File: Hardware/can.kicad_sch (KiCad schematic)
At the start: 11 parts, among them U2 SN65HVD230

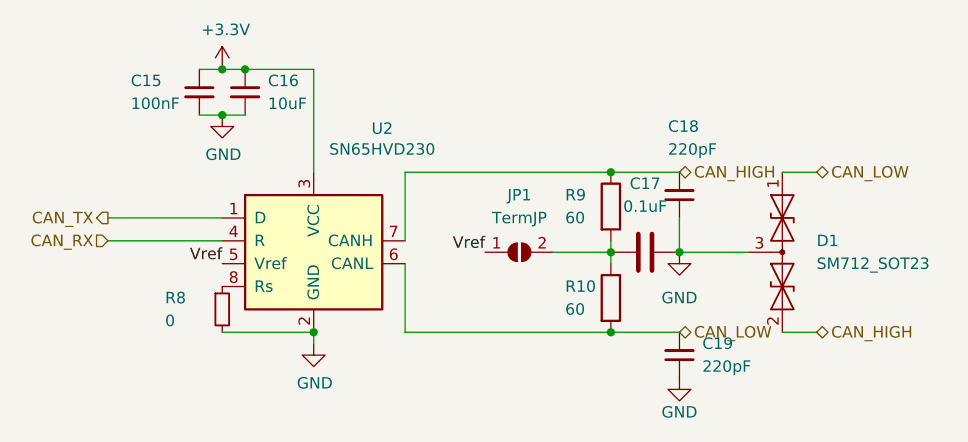
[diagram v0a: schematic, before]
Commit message: schematic done? + footprints assigned
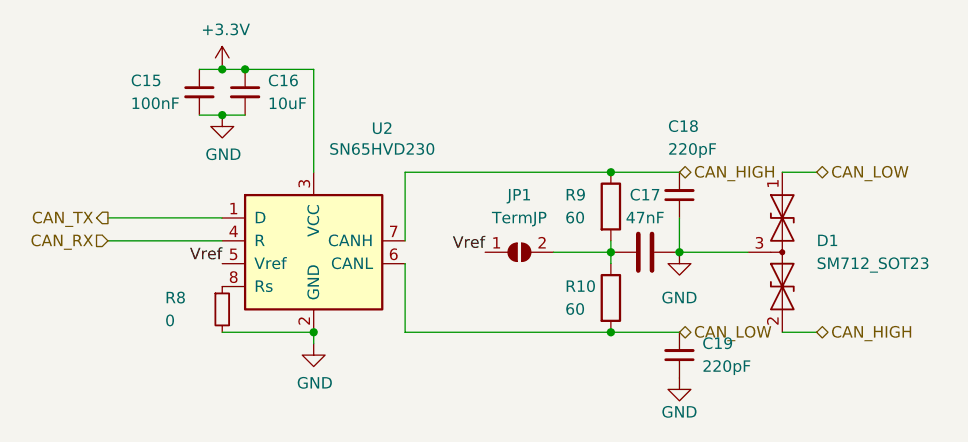
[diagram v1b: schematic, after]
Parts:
- C17: value 0.1uF -> 47nF
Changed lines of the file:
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@@
   (symbol (lib_id "Device:C") (at 171.45 88.9 90) (unit 1)
     (in_bom yes) (on_board yes) (dnp no) (fields_autoplaced)
-    (property "Reference" "C17" (at 171.45 81.28 90)
+    (property "Reference" "C17" (at 171.45 82.55 90)
       (effects (font (size 1.27 1.27)))
     )
-    (property "Value" "0.1uF" (at 171.45 83.82 90)
+    (property "Value" "47nF" (at 171.45 85.09 90)
       (effects (font (size 1.27 1.27)))
     )

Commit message: I had to get back out of bed to push this commit
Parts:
- JP1: footprint Jumper:SolderJumper-2_P1.3mm_Open_RoundedPad1.0x1.5mm -> iclr:SmallerSolderJP
- R10, R9: footprint Resistor_SMD:R_0402_1005Metric -> Resistor_SMD:R_0603_1608Metric
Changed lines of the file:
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@@
       (effects (font (size 1.27 1.27)) (justify left))
     )
-    (property "Footprint" "Resistor_SMD:R_0402_1005Metric" (at 165.862 93.98 90)
+    (property "Footprint" "Resistor_SMD:R_0603_1608Metric" (at 165.862 93.98 90)
       (effects (font (size 1.27 1.27)) hide)
     )
@@
       (effects (font (size 1.27 1.27)) (justify left))
     )
-    (property "Footprint" "Resistor_SMD:R_0402_1005Metric" (at 165.862 83.82 90)
+    (property "Footprint" "Resistor_SMD:R_0603_1608Metric" (at 165.862 83.82 90)
       (effects (font (size 1.27 1.27)) hide)
     )
@@
       (effects (font (size 1.27 1.27)))
     )
-    (property "Footprint" "Jumper:SolderJumper-2_P1.3mm_Open_RoundedPad1.0x1.5mm" (at 157.48 88.9 0)
+    (property "Footprint" "iclr:SmallerSolderJP" (at 157.48 88.9 0)
       (effects (font (size 1.27 1.27)) hide)
     )

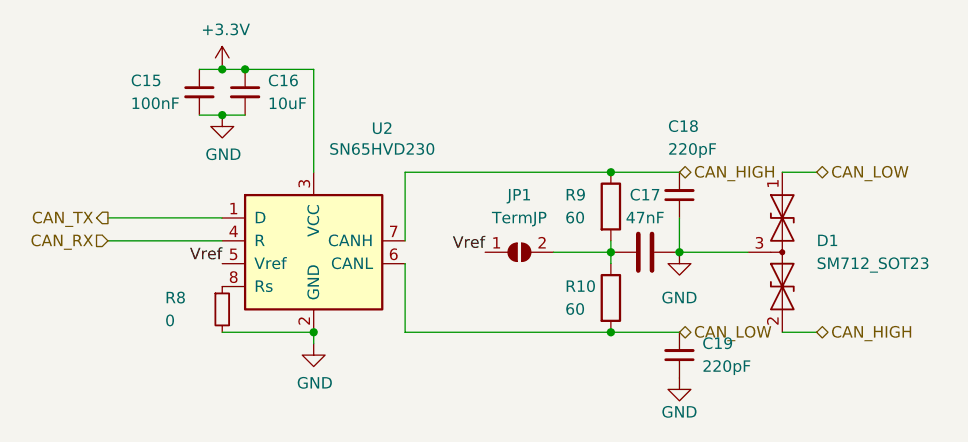
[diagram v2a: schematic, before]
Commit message: removed can caps, better via stitching, fini?
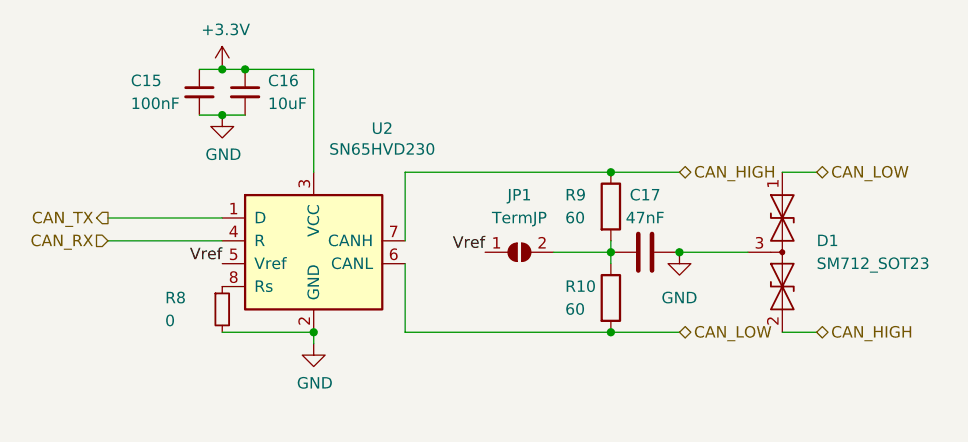
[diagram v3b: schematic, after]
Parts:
- removed C18, C19: 220pF, Capacitor_SMD:C_0402_1005Metric, symbol Device:C_Small
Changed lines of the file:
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@@
-    (stroke (width 0) (type default))
-  )
-  (wire (pts (xy 175.26 85.09) (xy 175.26 88.9))
     (stroke (width 0) (type default))
   )
@@
     )
   )
-  (symbol (lib_id "Device:C_Small") (at 175.26 82.55 180) (unit 1)
-    (in_bom yes) (on_board yes) (dnp no)
-    (property "Reference" "C18" (at 173.99 74.93 0)
-      (effects (font (size 1.27 1.27)) (justify right))
-    )
-    (property "Value" "220pF" (at 173.99 77.47 0)
-      (effects (font (size 1.27 1.27)) (justify right))
-    )
-    (property "Footprint" "Capacitor_SMD:C_0402_1005Metric" (at 175.26 82.55 0)
-      (effects (font (size 1.27 1.27)) hide)
-    )
-    (property "Datasheet" "~" (at 175.26 82.55 0)
-      (effects (font (size 1.27 1.27)) hide)
-    )
-    (pin "1")
-    (pin "2")
-    (instances
-      (project "flintandsteel"
-        (path "/7db990e4-92e1-4f99-b4d2-435bbec1ba83/00000000-0000-0000-0000-000061942b9a"
-          (reference "C18") (unit 1)
-        )
-      )
-    )
-  )
   (symbol (lib_id "Diode:SM712_SOT23") (at 186.69 88.9 270) (unit 1)
     (in_bom yes) (on_board yes) (dnp no) (fields_autoplaced)
@@
         (path "/7db990e4-92e1-4f99-b4d2-435bbec1ba83/00000000-0000-0000-0000-000061942b9a"
           (reference "#PWR027") (unit 1)
-        )
-      )
-    )
-  )
-  (symbol (lib_id "power:GND") (at 175.26 102.87 0) (unit 1)
-    (in_bom yes) (on_board yes) (dnp no) (fields_autoplaced)
-    (property "Reference" "#PWR028" (at 175.26 109.22 0)
-      (effects (font (size 1.27 1.27)) hide)
-    )
-    (property "Value" "GND" (at 175.26 106.68 0)
-      (effects (font (size 1.27 1.27)))
-    )
-    (property "Footprint" "" (at 175.26 102.87 0)
-      (effects (font (size 1.27 1.27)) hide)
-    )
-    (property "Datasheet" "" (at 175.26 102.87 0)
-      (effects (font (size 1.27 1.27)) hide)
-    )
-    (pin "1")
-    (instances
-      (project "flintandsteel"
-        (path "/7db990e4-92e1-4f99-b4d2-435bbec1ba83/00000000-0000-0000-0000-000061942b9a"
-          (reference "#PWR028") (unit 1)
         )
       )
@@
         )
       )
-    )
-  )
-  (symbol (lib_id "Device:C_Small") (at 175.26 100.33 180) (unit 1)
-    (in_bom yes) (on_board yes) (dnp no) (fields_autoplaced)
-    (property "Reference" "C19" (at 177.8 99.0535 0)
-      (effects (font (size 1.27 1.27)) (justify right))
-    )
-    (property "Value" "220pF" (at 177.8 101.5935 0)
-      (effects (font (size 1.27 1.27)) (justify right))
-    )
-    (property "Footprint" "Capacitor_SMD:C_0402_1005Metric" (at 175.26 100.33 0)
-      (effects (font (size 1.27 1.27)) hide)
-    )
-    (property "Datasheet" "~" (at 175.26 100.33 0)
-      (effects (font (size 1.27 1.27)) hide)
-    )
-    (pin "1")
-    (pin "2")
-    (instances
-      (project "flintandsteel"
-        (path "/7db990e4-92e1-4f99-b4d2-435bbec1ba83/00000000-0000-0000-0000-000061942b9a"
-          (reference "C19") (unit 1)
-        )
-      )
